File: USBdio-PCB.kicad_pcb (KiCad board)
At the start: 2 copper layers, 82.5 x 101.6 mm, 57 parts, among them IC1 ATMEGA328-P, IC2 CH340G, P0 RELAY_(JSM1A-12V-4), P1 RELAY_(JSM1A-12V-4), P2 RELAY_(JSM1A-12V-4), P3 RELAY_(JSM1A-12V-4), P4 RELAY_(JSM1A-12V-4), P5 RELAY_(JSM1A-12V-4), Q1 Q_NPN_BEC, Q12 Q_NPN, Q13 Q_NPN, Q14 Q_NPN, Q15 Q_NPN, Q16 Q_NPN, Q17 Q_NPN, Q4 Q_NPN_BEC, Q5 Q_NPN_BEC, Q6 Q_NPN_BEC, Q7 Q_NPN_BEC, Q8 Q_NPN_BEC, Q9 Q_NPN_BEC, U1 NCV7805BDTRKG, X1 Crystal_GND2, X2 Crystal_GND2

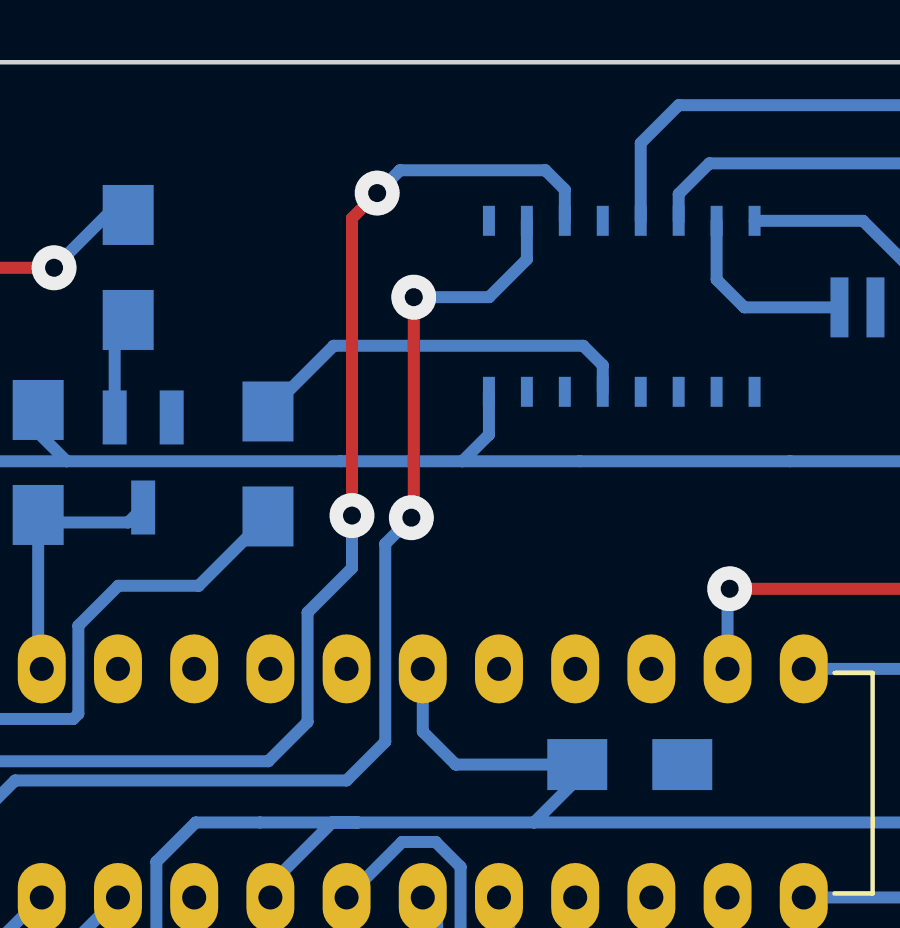
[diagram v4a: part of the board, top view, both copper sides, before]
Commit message: -Switched Tx and Rx. -Changed reset pull-up from 10kohm to 1kohm.
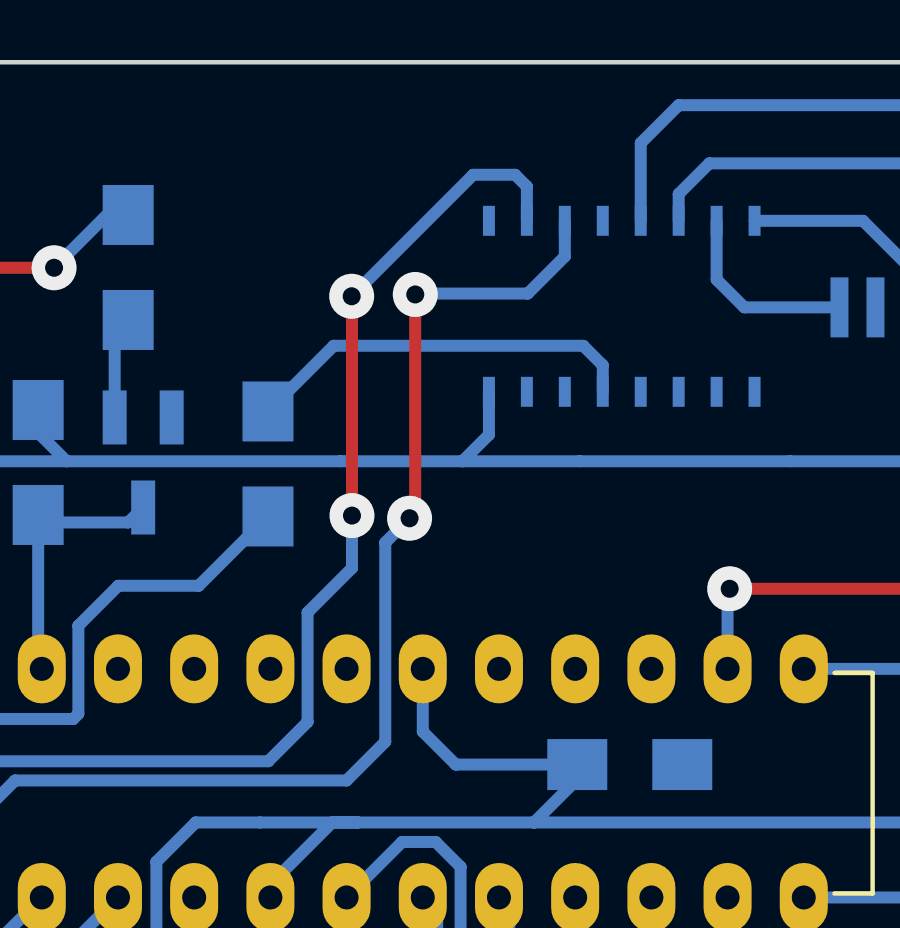
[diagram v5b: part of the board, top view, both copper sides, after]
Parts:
- R28: value 10k -> 1k
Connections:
- IC2 pad 2: TXD -> RXD
- IC2 pad 3: RXD -> TXD
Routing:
- net RXD: track 43.8 -> 40.9 mm
- net TXD: track 38.2 -> 39.5 mm
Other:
- net class High Amps: clearance 0.4 -> 0.2
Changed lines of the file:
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@@
-(kicad_pcb (version 4) (host pcbnew 4.0.6)
+(kicad_pcb (version 4) (host pcbnew 4.0.2-stable)
   (general
     (links 131)
@@
     (thickness 1.6)
     (drawings 6)
-    (tracks 446)
+    (tracks 448)
     (zones 0)
     (modules 57)
@@
   (page A4)
   (layers
-    (0 F.Cu signal hide)
+    (0 F.Cu signal)
     (31 B.Cu signal)
     (32 B.Adhes user)
@@
   )
   (net_class "High Amps" ""
-    (clearance 0.4)
+    (clearance 0.2)
     (trace_width 4.5)
     (via_dia 1.5)
@@
       (net 1 GND) (solder_mask_margin 0.2))
     (pad 2 smd rect (at -3.16 -2.845 180) (size 0.4 1) (layers B.Cu B.Paste B.Mask)
+      (net 56 RXD) (solder_mask_margin 0.2))
+    (pad 3 smd rect (at -1.895 -2.845 180) (size 0.4 1) (layers B.Cu B.Paste B.Mask)
       (net 58 TXD) (solder_mask_margin 0.2))
-    (pad 3 smd rect (at -1.895 -2.845 180) (size 0.4 1) (layers B.Cu B.Paste B.Mask)
-      (net 56 RXD) (solder_mask_margin 0.2))
     (pad 4 smd rect (at -0.63 -2.845 180) (size 0.4 1) (layers B.Cu B.Paste B.Mask)
       (net 65 "Net-(IC2-Pad4)") (solder_mask_margin 0.2))
@@
       (effects (font (size 1 1) (thickness 0.15)) (justify mirror))
     )
-    (fp_text value 10k (at 0 -1.9) (layer B.Fab)
+    (fp_text value 1k (at 0 -1.9) (layer B.Fab)
       (effects (font (size 1 1) (thickness 0.15)) (justify mirror))
     )
@@
   (segment (start 153.3526 107.2128) (end 133.0726 107.2128) (width 4.5) (layer B.Cu) (net 55))
   (segment (start 163.451 133.282) (end 180.211 133.282) (width 4.5) (layer B.Cu) (net 55))
-  (segment (start 132.6726 68.3228) (end 132.6726 66.7028) (width 0.4) (layer B.Cu) (net 56))
-  (segment (start 155.1876 44.7278) (end 155.1876 45.7678) (width 0.4) (layer B.Cu) (net 56))
-  (segment (start 154.5426 44.0828) (end 155.1876 44.7278) (width 0.4) (layer B.Cu) (net 56))
-  (segment (start 149.6926 44.0828) (end 154.5426 44.0828) (width 0.4) (layer B.Cu) (net 56))
-  (segment (start 148.9326 44.8428) (end 149.6926 44.0828) (width 0.4) (layer B.Cu) (net 56))
-  (via (at 148.9326 44.8428) (size 1.5) (drill 0.6) (layers F.Cu B.Cu) (net 56))
-  (segment (start 148.0926 45.6828) (end 148.9326 44.8428) (width 0.4) (layer F.Cu) (net 56))
-  (segment (start 148.0926 55.5928) (end 148.0926 45.6828) (width 0.4) (layer F.Cu) (net 56))
+  (segment (start 148.0926 55.5928) (end 148.0926 48.7928) (width 0.4) (layer F.Cu) (net 56))
+  (segment (start 132.6726 66.7028) (end 135.5926 63.7828) (width 0.4) (layer B.Cu) (net 56))
   (via (at 148.0926 55.5928) (size 1.5) (drill 0.6) (layers F.Cu B.Cu) (net 56))
   (segment (start 148.0926 57.3428) (end 148.0926 55.5928) (width 0.4) (layer B.Cu) (net 56))
@@
   (segment (start 145.3026 63.7828) (end 146.6126 62.4728) (width 0.4) (layer B.Cu) (net 56))
   (segment (start 135.5926 63.7828) (end 145.3026 63.7828) (width 0.4) (layer B.Cu) (net 56))
-  (segment (start 132.6726 66.7028) (end 135.5926 63.7828) (width 0.4) (layer B.Cu) (net 56))
+  (segment (start 132.6726 68.3228) (end 132.6726 66.7028) (width 0.4) (layer B.Cu) (net 56))
+  (segment (start 153.9226 44.6228) (end 153.9226 45.7678) (width 0.4) (layer B.Cu) (net 56))
+  (segment (start 153.5326 44.2328) (end 153.9226 44.6228) (width 0.4) (layer B.Cu) (net 56))
+  (segment (start 152.1326 44.2328) (end 153.5326 44.2328) (width 0.4) (layer B.Cu) (net 56))
+  (segment (start 148.0826 48.2828) (end 152.1326 44.2328) (width 0.4) (layer B.Cu) (net 56))
+  (via (at 148.0826 48.2828) (size 1.5) (drill 0.6) (layers F.Cu B.Cu) (net 56))
+  (segment (start 148.0826 48.7828) (end 148.0826 48.2828) (width 0.4) (layer F.Cu) (net 56))
+  (segment (start 148.0926 48.7928) (end 148.0826 48.7828) (width 0.4) (layer F.Cu) (net 56))
   (segment (start 154.4526 136.5728) (end 154.4526 85.4428) (width 0.4) (layer F.Cu) (net 57))
   (segment (start 184.401 133.282) (end 184.401 135.5944) (width 0.4) (layer F.Cu) (net 57))
@@
   (segment (start 184.401 135.5944) (end 182.3126 137.6828) (width 0.4) (layer F.Cu) (net 57))
   (segment (start 139.1326 79.2328) (end 139.1326 79.1428) (width 0.4) (layer B.Cu) (net 57))
+  (segment (start 149.2026 63.1328) (end 149.2026 56.4928) (width 0.4) (layer B.Cu) (net 58))
+  (segment (start 135.2126 66.0728) (end 136.8626 64.4228) (width 0.4) (layer B.Cu) (net 58))
   (segment (start 135.2126 68.3228) (end 135.2126 66.0728) (width 0.4) (layer B.Cu) (net 58))
-  (segment (start 153.9226 47.0528) (end 153.9226 45.7678) (width 0.4) (layer B.Cu) (net 58))
-  (segment (start 152.6626 48.3128) (end 153.9226 47.0528) (width 0.4) (layer B.Cu) (net 58))
-  (segment (start 150.1526 48.3128) (end 152.6626 48.3128) (width 0.4) (layer B.Cu) (net 58))
-  (via (at 150.1526 48.3128) (size 1.5) (drill 0.6) (layers F.Cu B.Cu) (net 58))
-  (segment (start 150.1526 55.5828) (end 150.1526 48.3128) (width 0.4) (layer F.Cu) (net 58))
-  (segment (start 150.0726 55.6628) (end 150.1526 55.5828) (width 0.4) (layer F.Cu) (net 58))
-  (via (at 150.0726 55.6628) (size 1.5) (drill 0.6) (layers F.Cu B.Cu) (net 58))
-  (segment (start 149.2026 56.5328) (end 150.0726 55.6628) (width 0.4) (layer B.Cu) (net 58))
-  (segment (start 149.2026 63.1328) (end 149.2026 56.5328) (width 0.4) (layer B.Cu) (net 58))
+  (segment (start 136.8626 64.4228) (end 147.9126 64.4228) (width 0.4) (layer B.Cu) (net 58))
   (segment (start 147.9126 64.4228) (end 149.2026 63.1328) (width 0.4) (layer B.Cu) (net 58))
-  (segment (start 136.8626 64.4228) (end 147.9126 64.4228) (width 0.4) (layer B.Cu) (net 58))
-  (segment (start 135.2126 66.0728) (end 136.8626 64.4228) (width 0.4) (layer B.Cu) (net 58))
+  (segment (start 155.1876 46.9578) (end 155.1876 45.7678) (width 0.4) (layer B.Cu) (net 58))
+  (segment (start 153.9526 48.1928) (end 155.1876 46.9578) (width 0.4) (layer B.Cu) (net 58))
+  (segment (start 150.2326 48.1928) (end 153.9526 48.1928) (width 0.4) (layer B.Cu) (net 58))
+  (segment (start 150.2026 48.2228) (end 150.2326 48.1928) (width 0.4) (layer B.Cu) (net 58))
+  (via (at 150.2026 48.2228) (size 1.5) (drill 0.6) (layers F.Cu B.Cu) (net 58))
+  (segment (start 150.2026 55.4928) (end 150.2026 48.2228) (width 0.4) (layer F.Cu) (net 58))
+  (segment (start 150.0126 55.6828) (end 150.2026 55.4928) (width 0.4) (layer F.Cu) (net 58))
+  (via (at 150.0126 55.6828) (size 1.5) (drill 0.6) (layers F.Cu B.Cu) (net 58))
+  (segment (start 149.2026 56.4928) (end 150.0126 55.6828) (width 0.4) (layer B.Cu) (net 58))
   (segment (start 168.5326 102.6528) (end 175.5226 95.6628) (width 0.4) (layer B.Cu) (net 59))
   (segment (start 175.5226 67.5928) (end 178.2426 64.8728) (width 0.4) (layer B.Cu) (net 59))
